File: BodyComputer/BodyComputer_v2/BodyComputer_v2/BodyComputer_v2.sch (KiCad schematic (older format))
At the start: 0 parts

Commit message: Second version of the body computer - WIP
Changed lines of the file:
@@
 $Descr A3 16535 11693
 encoding utf-8
-Sheet 1 3
+Sheet 1 9
 Title ""
 Date ""
@@
 $EndDescr
 $Sheet
-S 7350 4450 1500 2950
+S 6000 2000 3000 7500
 U 5FAC00ED
 F0 "MCU" 50
@@
 $EndSheet
 $Sheet
-S 11700 3950 1100 1400
+S 12000 4500 1500 1000
 U 60EBB99E
 F0 "PowerSupply" 50
 F1 "PowerSupply.sch" 50
+F2 "5V_DCDC_ENABLE" I L 12000 4600 50
+F3 "ADC_BOARD_TEMP_1" I L 12000 4750 50
+F4 "ADC_BOARD_TEMP_2" I L 12000 4850 50
+F5 "ADC_BOARD_TEMP_3" I L 12000 4950 50
+F6 "ADC_3V3" I L 12000 5100 50
+F7 "ADC_5V" I L 12000 5200 50
+F8 "ADC_VIN" I L 12000 5300 50
+$EndSheet
+$Sheet
+S 12000 6000 1500 1500
+U 602025D1
+F0 "Memory" 50
+F1 "Memory.sch" 50
+F2 "EEPROM_SDA" I L 12000 6100 50
+F3 "EEPROM_SCL" I L 12000 6200 50
+F4 "EEPROM_WP1" I L 12000 6300 50
+F5 "SDIO_DATA2" I L 12000 6850 50
+F6 "SDIO_DATA3" I L 12000 6950 50
+F7 "SDIO_CMD" I L 12000 7050 50
+F8 "SDIO_CLK" I L 12000 7150 50
+F9 "SDIO_DATA1" I L 12000 6750 50
+F10 "SDIO_DATA0" I L 12000 6650 50
+F11 "MICROSD_DETECT" I L 12000 7250 50
+F12 "PowerOn_MICROSD" I L 12000 6550 50
+F13 "EEPROM_WP2" I L 12000 6400 50
+$EndSheet
+$Sheet
+S 12000 8000 900  1300
+U 602F5758
+F0 "Pulls_and_TestPoints" 50
+F1 "Pulls_and_TestPoints.sch" 50
+$EndSheet
+$Sheet
+S 12000 2000 1500 2000
+U 60482FFF
+F0 "Peripherals" 50
+F1 "Peripherals.sch" 50
+F2 "TX_GPS" I L 12000 2200 50
+F3 "RX_GPS" I L 12000 2100 50
+F4 "PowerOn_GPS" I L 12000 2300 50
+F5 "BUZZER" I L 12000 2450 50
+F6 "USB_DP" I L 12000 2600 50
+F7 "USB_DN" I L 12000 2700 50
+F8 "RESET_BUTTON" I L 12000 2950 50
+F9 "PowerOn_LCD" I L 12000 3100 50
+F10 "SCL_LCD" I L 12000 3200 50
+F11 "SDA_LCD" I L 12000 3300 50
+F12 "RX_NODEMCU" I L 12000 3550 50
+F13 "TX_NODEMCU" I L 12000 3650 50
+F14 "PowerOn_NODEMCU" I L 12000 3750 50
+F15 "EXTERNAL_RESET" I L 12000 3850 50
+F16 "PWM_BACKLIGHT_LCD" I L 12000 3400 50
+F17 "USB_ID" I L 12000 2800 50
+$EndSheet
+$Sheet
+S 2000 2000 1500 1500
+U 61744C84
+F0 "CruiseControl" 50
+F1 "CruiseControl.sch" 50
+F2 "PowerOn_CRUISE_CONTROL" I R 3500 2100 50
+F3 "IN1_ENGINE" I R 3500 2300 50
+F4 "IN2_ENGINE" I R 3500 2400 50
+F5 "EN_ELECTRO_CLUTCH" I R 3500 2500 50
+F6 "ENC1_BUTTON" I R 3500 2650 50
+F7 "ENC1_CH_A" I R 3500 2750 50
+F8 "ENC1_CH_B" I R 3500 2850 50
+F9 "ENC2_BUTTON" I R 3500 3000 50
+F10 "ENC2_CH_A" I R 3500 3100 50
+F11 "ENC2_CH_B" I R 3500 3200 50
+F12 "PWM_EN_ENGINE" I R 3500 2200 50
+$EndSheet
+$Sheet
+S 2000 4000 1500 4000
+U 61D91431
+F0 "Measurements" 50
+F1 "Measurements.sch" 50
+F2 "OIL_PRESSURE_BINARY" I R 3500 5850 50
+F3 "CLUTCH_PEDAL" I R 3500 6700 50
+F4 "BRAKE_PEDAL" I R 3500 6600 50
+F5 "RPM" I R 3500 6850 50
+F6 "ALTERNATOR_CHARGING" I R 3500 5950 50
+F7 "SPEED" I R 3500 6950 50
+F8 "KEY_IGNITION" I R 3500 6350 50
+F9 "KEY_CRANKING" I R 3500 6450 50
+F10 "ADC_LM35_1_N" I R 3500 4100 50
+F11 "ADC_LM35_1_P" I R 3500 4200 50
+F12 "ADC_LM35_2_P" I R 3500 4300 50
+F13 "ADC_LM35_2_N" I R 3500 4400 50
+F14 "ADC_ACC_POSITION" I R 3500 5650 50
+F15 "ADC_FUEL_POSITION" I R 3500 5750 50
+F16 "ADC_LM35_3_P" I R 3500 4500 50
+F17 "ADC_LM35_3_N" I R 3500 4600 50
+F18 "ADC_LM35_4_N" I R 3500 4800 50
+F19 "ADC_LM35_4_P" I R 3500 4700 50
+F20 "ADC_LM35_5_P" I R 3500 4900 50
+F21 "ADC_LM35_5_N" I R 3500 5000 50
+F22 "ADC_POTENTIOMETER_1" I R 3500 5400 50
+F23 "ADC_RESISTANCE_SENS_1" I R 3500 5150 50
+F24 "ADC_RESISTANCE_SENS_2" I R 3500 5250 50
+F25 "ADC_POTENTIOMETER_2" I R 3500 5500 50
+F26 "IN_BIN_1" I R 3500 7100 50
+F27 "IN_BIN_2" I R 3500 7200 50
+F28 "IN_BIN_3" I R 3500 7300 50
+F29 "IN_BIN_4" I R 3500 7400 50
+F30 "IN_BIN_5" I R 3500 7500 50
+F31 "IN_BIN_6" I R 3500 7600 50
+F32 "IN_BIN_7" I R 3500 7700 50
+F33 "IN_BIN_8" I R 3500 7800 50
+F34 "ADC_MAIN_BATTERY" I R 3500 6050 50
+F35 "ADC_AUX_BATTERY" I R 3500 6150 50
+$EndSheet
+$Sheet
+S 2000 8500 1500 1500
+U 634E5A89
+F0 "Controls" 50
+F1 "Controls.sch" 50
 $EndSheet
 $EndSCHEMATC

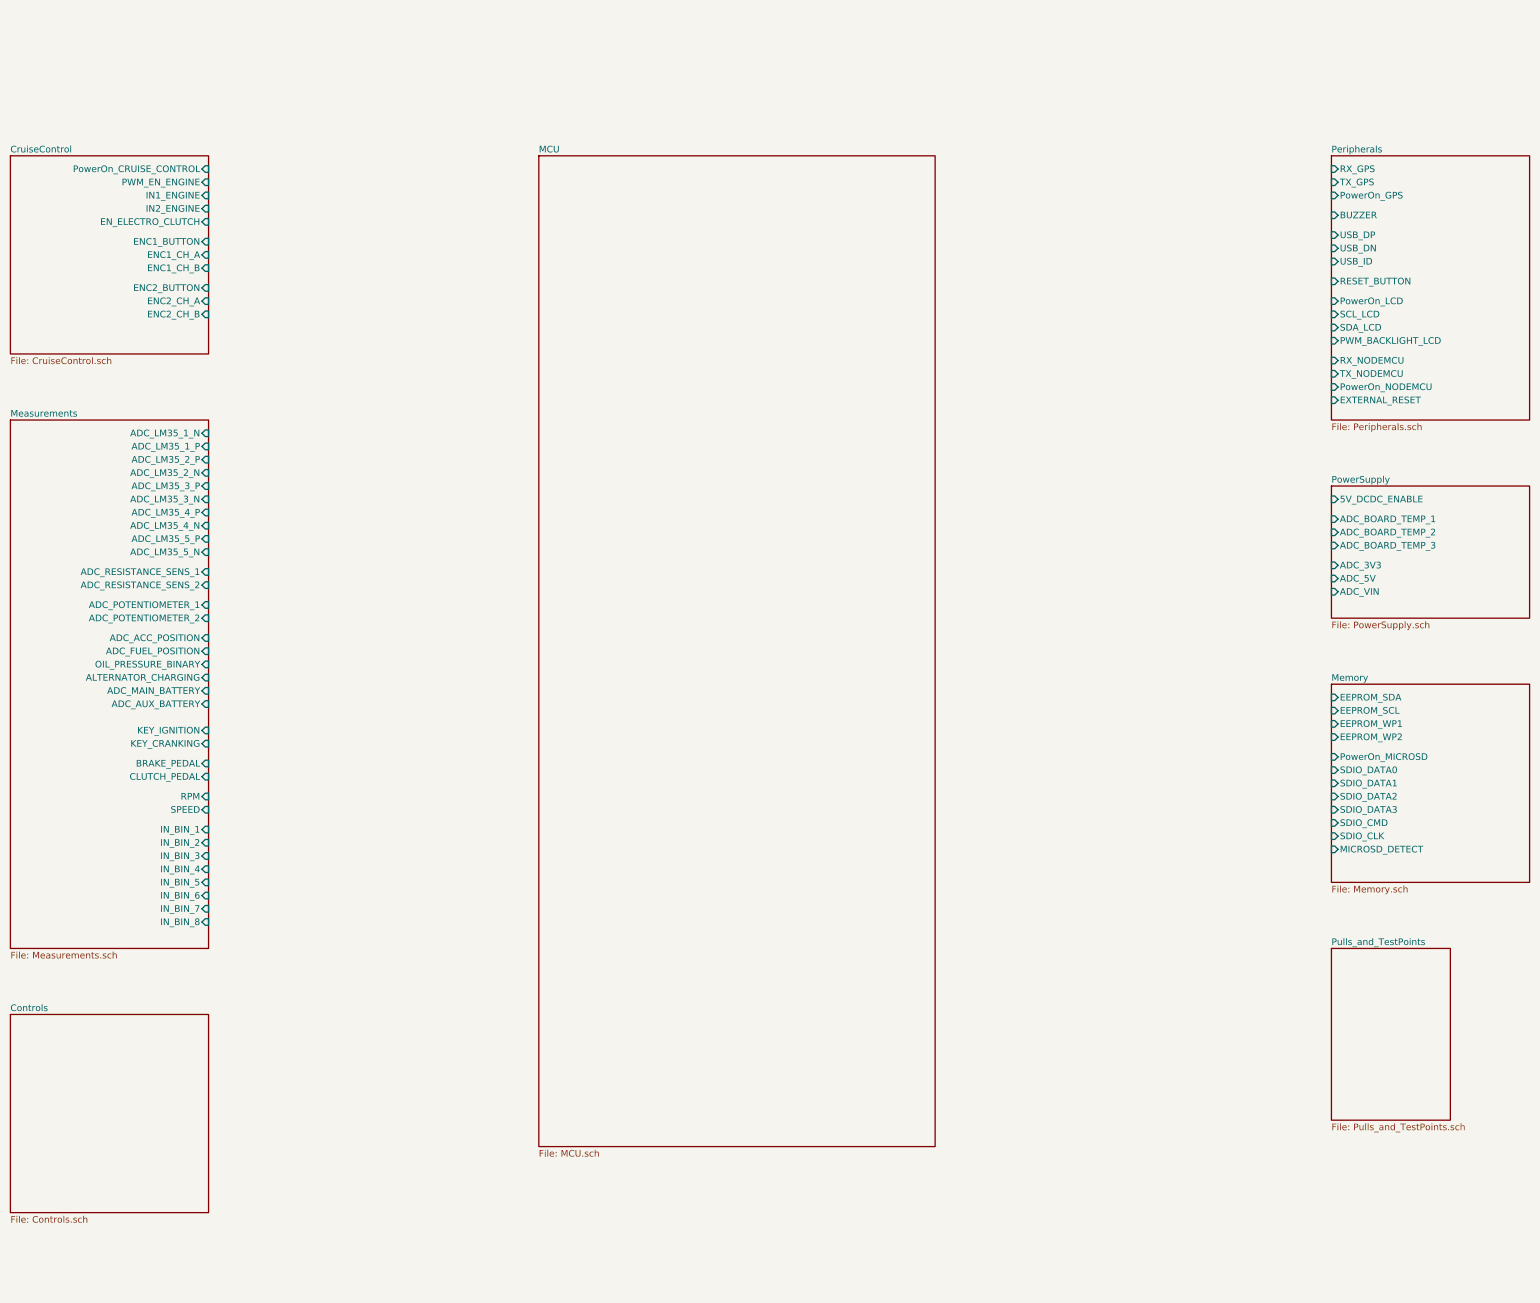
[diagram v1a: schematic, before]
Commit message: Finished board design. Schematic names improvements needed.
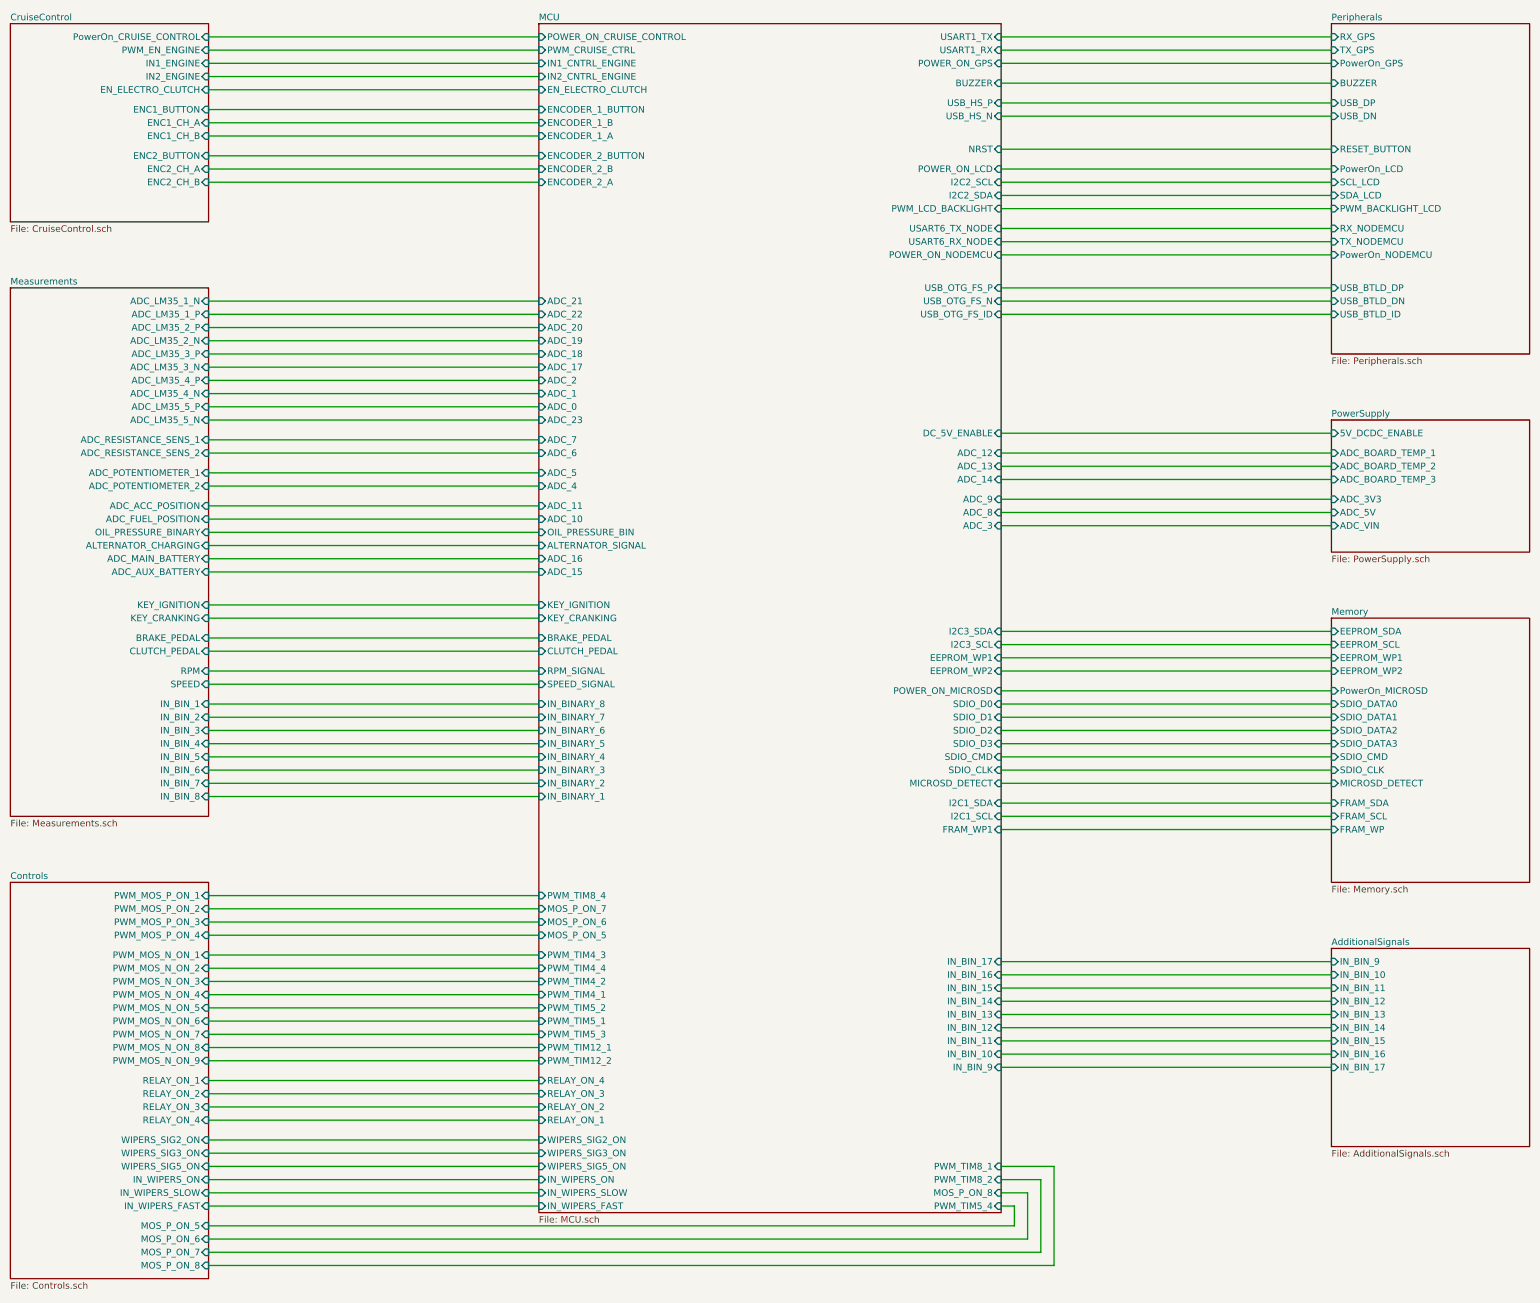
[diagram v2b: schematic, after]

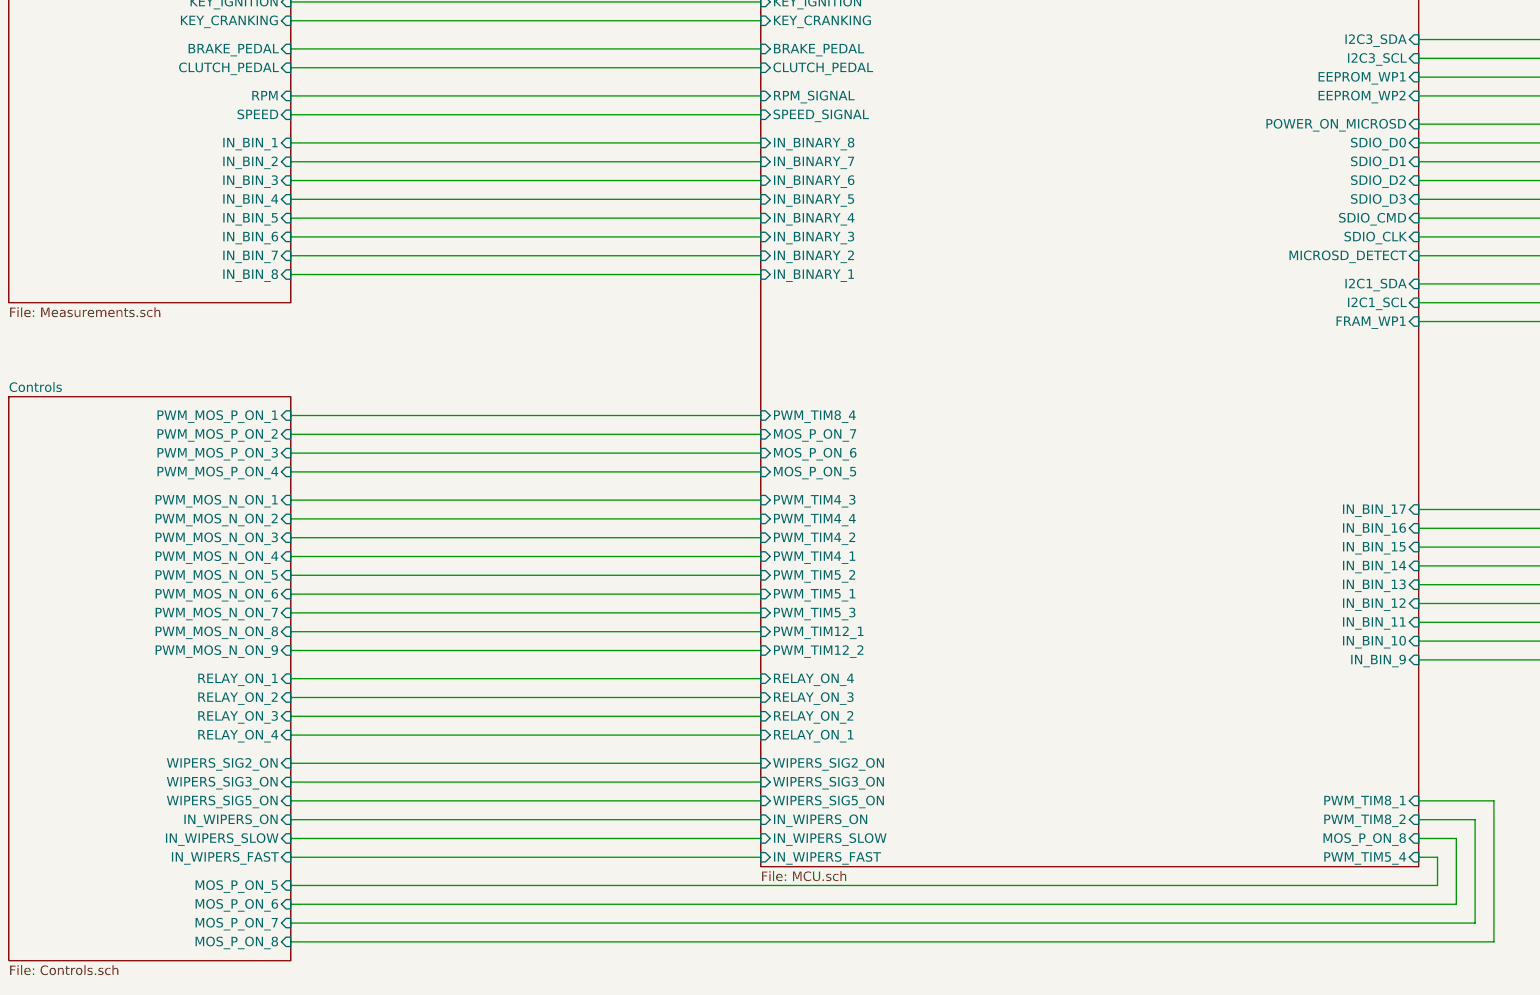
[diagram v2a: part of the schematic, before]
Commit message: Signals naming improvements
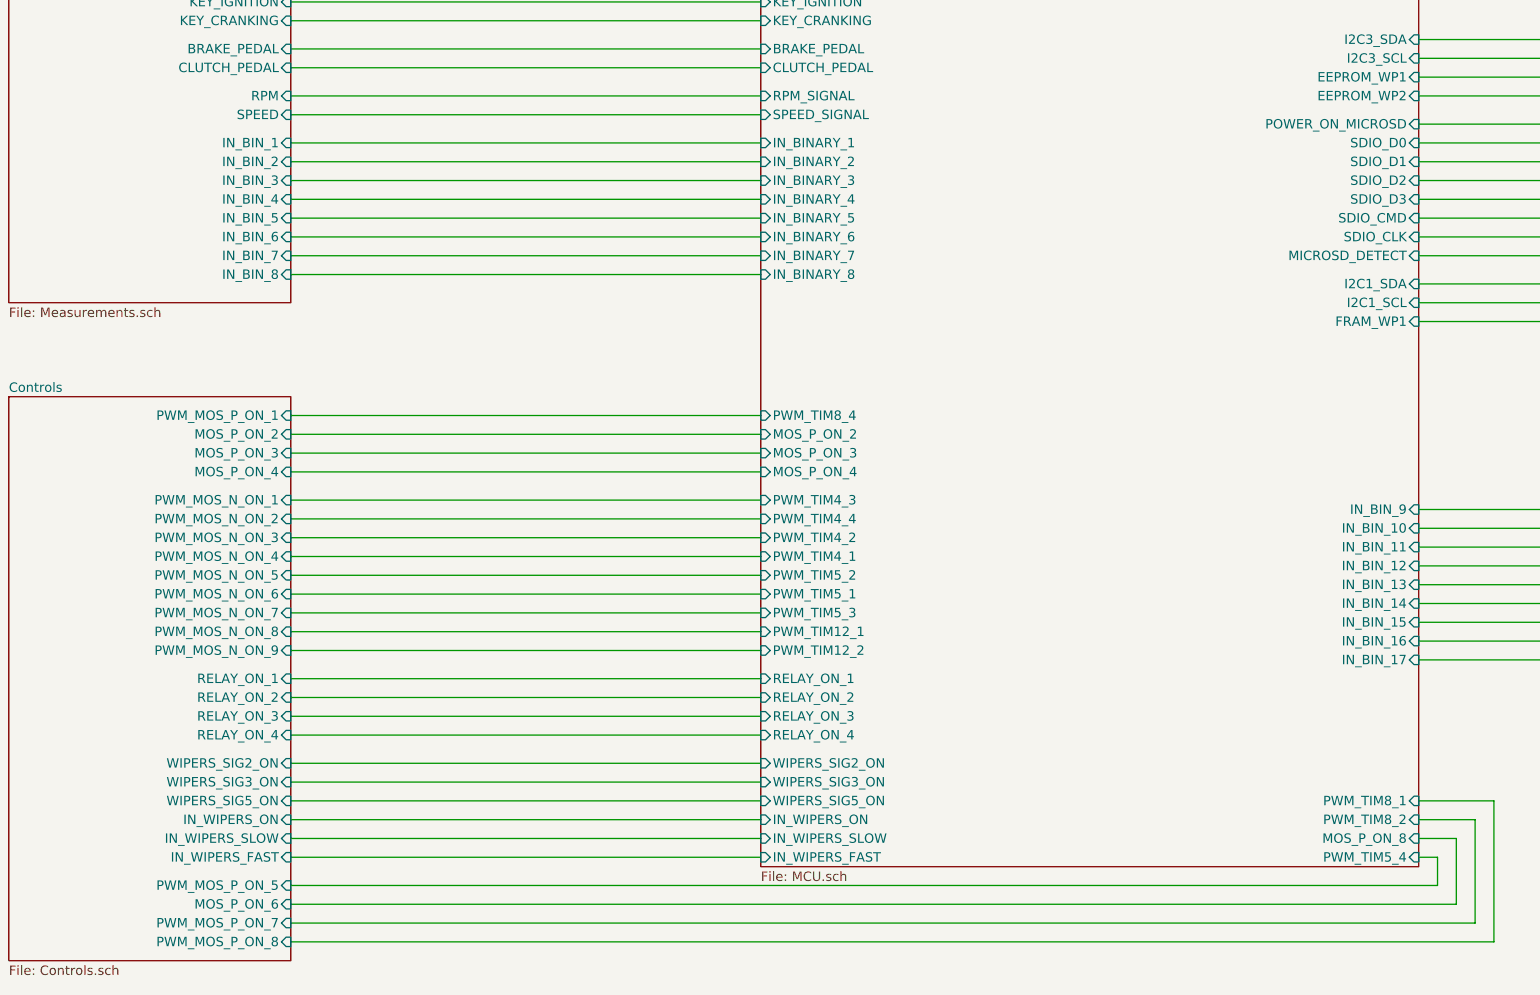
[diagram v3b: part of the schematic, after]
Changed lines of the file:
@@
 F1 "Controls.sch" 50
 F2 "PWM_MOS_P_ON_1" I R 3500 7600 50
-F3 "PWM_MOS_P_ON_2" I R 3500 7700 50
-F4 "PWM_MOS_P_ON_3" I R 3500 7800 50
-F5 "PWM_MOS_P_ON_4" I R 3500 7900 50
-F6 "PWM_MOS_N_ON_1" I R 3500 8050 50
-F7 "PWM_MOS_N_ON_2" I R 3500 8150 50
-F8 "PWM_MOS_N_ON_3" I R 3500 8250 50
-F9 "PWM_MOS_N_ON_4" I R 3500 8350 50
-F10 "PWM_MOS_N_ON_5" I R 3500 8450 50
-F11 "PWM_MOS_N_ON_6" I R 3500 8550 50
-F12 "PWM_MOS_N_ON_7" I R 3500 8650 50
-F13 "PWM_MOS_N_ON_8" I R 3500 8750 50
-F14 "PWM_MOS_N_ON_9" I R 3500 8850 50
-F15 "RELAY_ON_1" I R 3500 9000 50
-F16 "WIPERS_SIG2_ON" I R 3500 9450 50
-F17 "WIPERS_SIG3_ON" I R 3500 9550 50
-F18 "WIPERS_SIG5_ON" I R 3500 9650 50
-F19 "IN_WIPERS_ON" I R 3500 9750 50
-F20 "IN_WIPERS_SLOW" I R 3500 9850 50
-F21 "IN_WIPERS_FAST" I R 3500 9950 50
-F22 "RELAY_ON_2" I R 3500 9100 50
-F23 "RELAY_ON_3" I R 3500 9200 50
-F24 "RELAY_ON_4" I R 3500 9300 50
-F25 "MOS_P_ON_5" I R 3500 10100 50
-F26 "MOS_P_ON_6" I R 3500 10200 50
-F27 "MOS_P_ON_7" I R 3500 10300 50
-F28 "MOS_P_ON_8" I R 3500 10400 50
+F3 "PWM_MOS_N_ON_1" I R 3500 8050 50
+F4 "PWM_MOS_N_ON_2" I R 3500 8150 50
+F5 "PWM_MOS_N_ON_3" I R 3500 8250 50
+F6 "PWM_MOS_N_ON_4" I R 3500 8350 50
+F7 "PWM_MOS_N_ON_5" I R 3500 8450 50
+F8 "PWM_MOS_N_ON_6" I R 3500 8550 50
+F9 "PWM_MOS_N_ON_7" I R 3500 8650 50
+F10 "PWM_MOS_N_ON_8" I R 3500 8750 50
+F11 "PWM_MOS_N_ON_9" I R 3500 8850 50
+F12 "RELAY_ON_1" I R 3500 9000 50
+F13 "WIPERS_SIG2_ON" I R 3500 9450 50
+F14 "WIPERS_SIG3_ON" I R 3500 9550 50
+F15 "WIPERS_SIG5_ON" I R 3500 9650 50
+F16 "IN_WIPERS_ON" I R 3500 9750 50
+F17 "IN_WIPERS_SLOW" I R 3500 9850 50
+F18 "IN_WIPERS_FAST" I R 3500 9950 50
+F19 "RELAY_ON_2" I R 3500 9100 50
+F20 "RELAY_ON_3" I R 3500 9200 50
+F21 "RELAY_ON_4" I R 3500 9300 50
+F22 "MOS_P_ON_6" I R 3500 10200 50
+F23 "MOS_P_ON_2" I R 3500 7700 50
+F24 "MOS_P_ON_3" I R 3500 7800 50
+F25 "MOS_P_ON_4" I R 3500 7900 50
+F26 "PWM_MOS_P_ON_5" I R 3500 10100 50
+F27 "PWM_MOS_P_ON_7" I R 3500 10300 50
+F28 "PWM_MOS_P_ON_8" I R 3500 10400 50
 $EndSheet
 Wire Wire Line
@@
 F82 "OIL_PRESSURE_BIN" I L 6000 4850 50
 F83 "CLUTCH_PEDAL" I L 6000 5750 50
-F84 "IN_BINARY_1" I L 6000 6850 50
-F85 "IN_BINARY_2" I L 6000 6750 50
-F86 "IN_BINARY_3" I L 6000 6650 50
-F87 "IN_BINARY_4" I L 6000 6550 50
-F88 "IN_BINARY_5" I L 6000 6450 50
-F89 "IN_BINARY_6" I L 6000 6350 50
-F90 "IN_BINARY_7" I L 6000 6250 50
-F91 "IN_BINARY_8" I L 6000 6150 50
+F84 "IN_BINARY_1" I L 6000 6150 50
+F85 "IN_BINARY_2" I L 6000 6250 50
+F86 "IN_BINARY_3" I L 6000 6350 50
+F87 "IN_BINARY_4" I L 6000 6450 50
+F88 "IN_BINARY_5" I L 6000 6550 50
+F89 "IN_BINARY_6" I L 6000 6650 50
+F90 "IN_BINARY_7" I L 6000 6750 50
+F91 "IN_BINARY_8" I L 6000 6850 50
 F92 "EN_ELECTRO_CLUTCH" I L 6000 1500 50
 F93 "IN2_CNTRL_ENGINE" I L 6000 1400 50
@@
 F100 "WIPERS_SIG3_ON" I L 6000 9550 50
 F101 "WIPERS_SIG2_ON" I L 6000 9450 50
-F102 "RELAY_ON_1" I L 6000 9300 50
-F103 "RELAY_ON_2" I L 6000 9200 50
-F104 "RELAY_ON_3" I L 6000 9100 50
-F105 "RELAY_ON_4" I L 6000 9000 50
-F106 "DC_5V_ENABLE" I R 9500 4100 50
-F107 "BUZZER" I R 9500 1450 50
-F108 "POWER_ON_MICROSD" I R 9500 6050 50
-F109 "MOS_P_ON_5" I L 6000 7900 50
-F110 "MOS_P_ON_6" I L 6000 7800 50
-F111 "MOS_P_ON_7" I L 6000 7700 50
-F112 "MOS_P_ON_8" I R 9500 9850 50
-F113 "IN_BIN_9" I R 9500 8900 50
-F114 "IN_BIN_10" I R 9500 8800 50
-F115 "IN_BIN_11" I R 9500 8700 50
-F116 "IN_BIN_12" I R 9500 8600 50
-F117 "IN_BIN_13" I R 9500 8500 50
-F118 "IN_BIN_14" I R 9500 8400 50
-F119 "IN_BIN_15" I R 9500 8300 50
-F120 "IN_BIN_16" I R 9500 8200 50
-F121 "IN_BIN_17" I R 9500 8100 50
+F102 "RELAY_ON_1" I L 6000 9000 50
+F103 "RELAY_ON_2" I L 6000 9100 50
+F104 "RELAY_ON_3" I L 6000 9200 50
+F105 "DC_5V_ENABLE" I R 9500 4100 50
+F106 "BUZZER" I R 9500 1450 50
+F107 "POWER_ON_MICROSD" I R 9500 6050 50
+F108 "MOS_P_ON_8" I R 9500 9850 50
+F109 "IN_BIN_9" I R 9500 8100 50
+F110 "IN_BIN_10" I R 9500 8200 50
+F111 "IN_BIN_11" I R 9500 8300 50
+F112 "IN_BIN_12" I R 9500 8400 50
+F113 "IN_BIN_13" I R 9500 8500 50
+F114 "IN_BIN_14" I R 9500 8600 50
+F115 "IN_BIN_15" I R 9500 8700 50
+F116 "IN_BIN_16" I R 9500 8800 50
+F117 "IN_BIN_17" I R 9500 8900 50
+F118 "MOS_P_ON_2" I L 6000 7700 50
+F119 "MOS_P_ON_3" I L 6000 7800 50
+F120 "MOS_P_ON_4" I L 6000 7900 50
+F121 "RELAY_ON_4" I L 6000 9300 50
 $EndSheet
 $EndSCHEMATC
